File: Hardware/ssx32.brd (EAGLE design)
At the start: 61 x 60 mm, 81 parts, among them IC1 PIC18F45K20, IC2 FT232RL, IC3 TXB0108PW, IC4 TXB0108PW, IC5 TXB0108PW, IC6 TXB0108PW, IC7 78L33, IC8 74AHC1G32DBV, X1 8, X10 1, X11 19, X12 16, X13 15, X14 14, X15 13, X16 12, X17 11, X18 10, X19 9, X20 20, X21 21, X22 22, X23 23, X24 24, X25 25, X26 26, X27 27, X28 28, X29 29, X3 17, X30 30, X31 31, X32 32, X33 1751248, X34 18, X35 USB, X4 7, X5 6, X6 5, X7 4, X8 3, X9 2

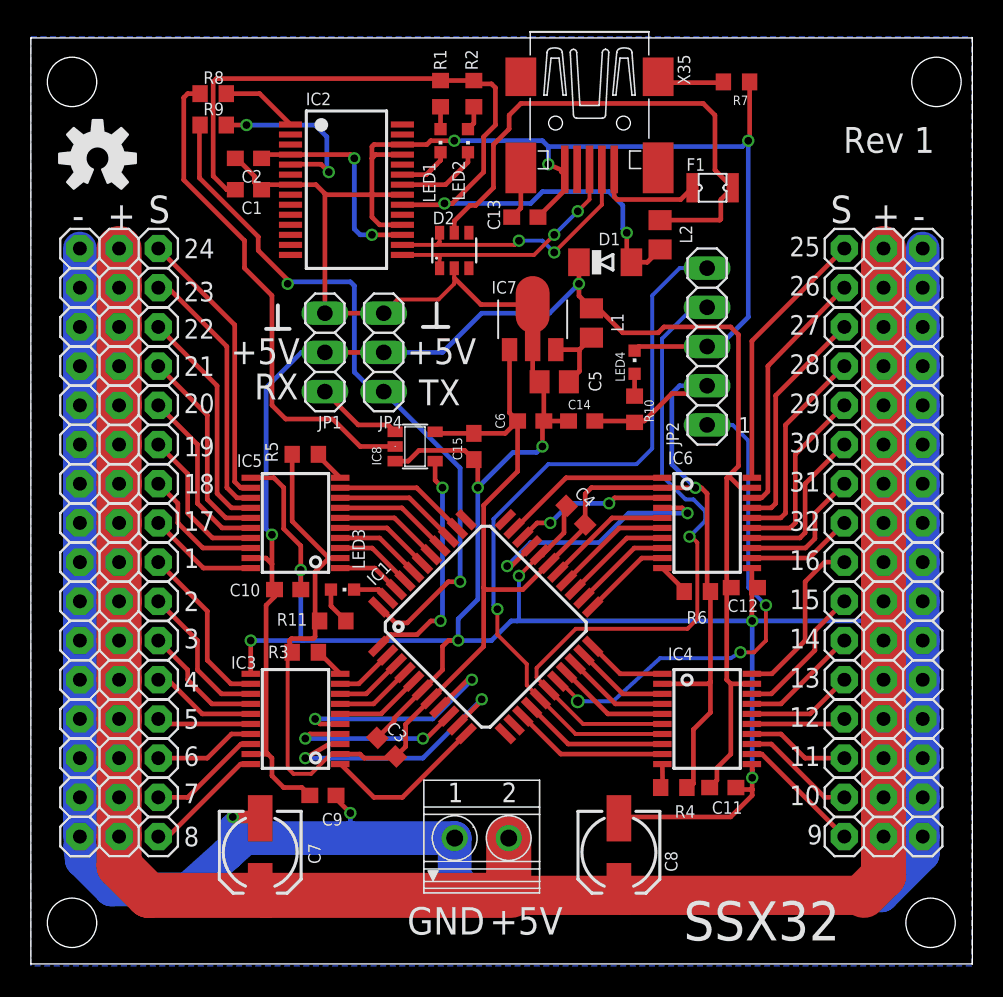
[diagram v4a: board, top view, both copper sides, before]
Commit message: Added software, minor board changes
Added software
Added resistor for not mounted ftdi chip
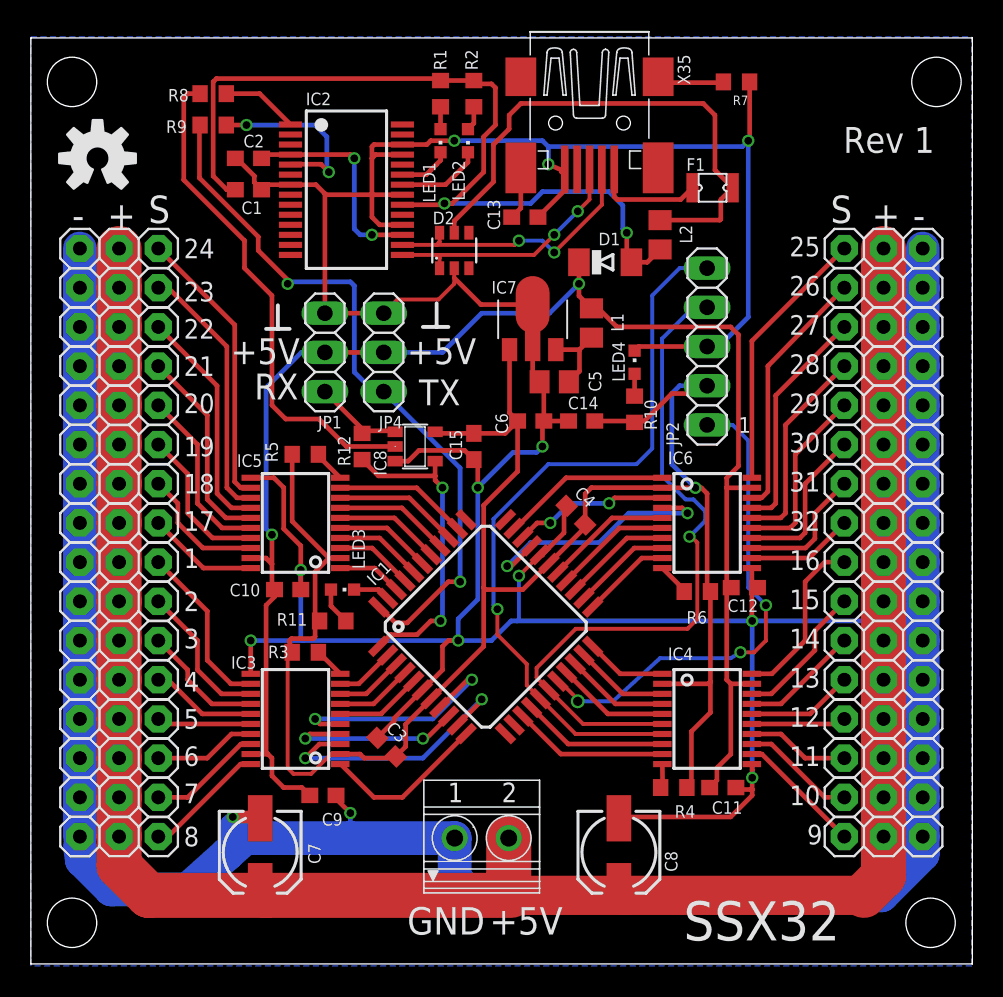
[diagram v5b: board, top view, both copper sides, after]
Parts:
- added R12: 0, rcl:R0603
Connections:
- net N$48: now also R12.1
- net N$54: now also R12.2
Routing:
- net N$48: track 15.3 -> 20.5 mm
- net +UB: track 102.6 -> 102.1 mm

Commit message: Revert "Added software, minor board changes"
This reverts commit cd959f70c37cd81d74ff6deb02d888d0a529ccba.
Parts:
- removed R12: 0, rcl:R0603
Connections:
- net N$48: no longer R12.1
- net N$54: no longer R12.2
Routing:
- net N$48: track 20.5 -> 15.3 mm
- net +UB: track 102.1 -> 102.6 mm

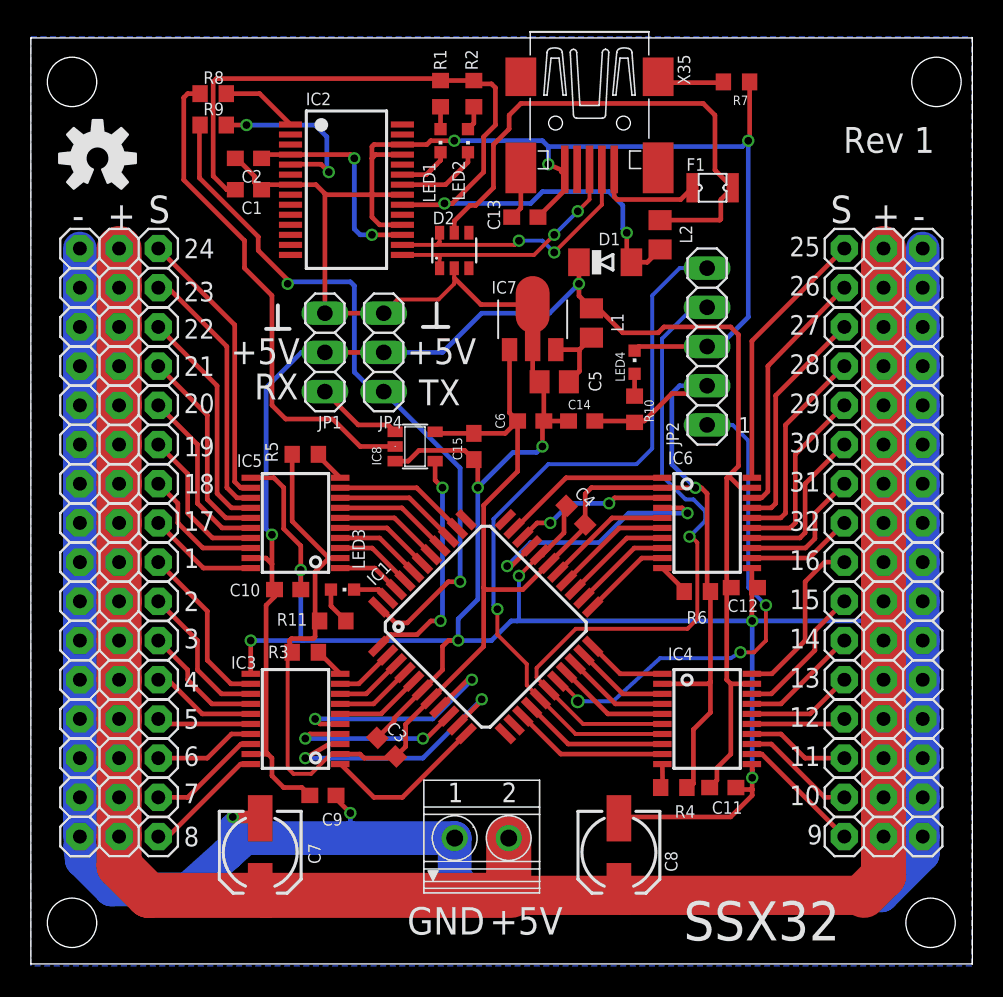
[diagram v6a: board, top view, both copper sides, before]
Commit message: Fixed issues
Replaced OR with AND gate with pullups
Removed unnecessary ferrite bead
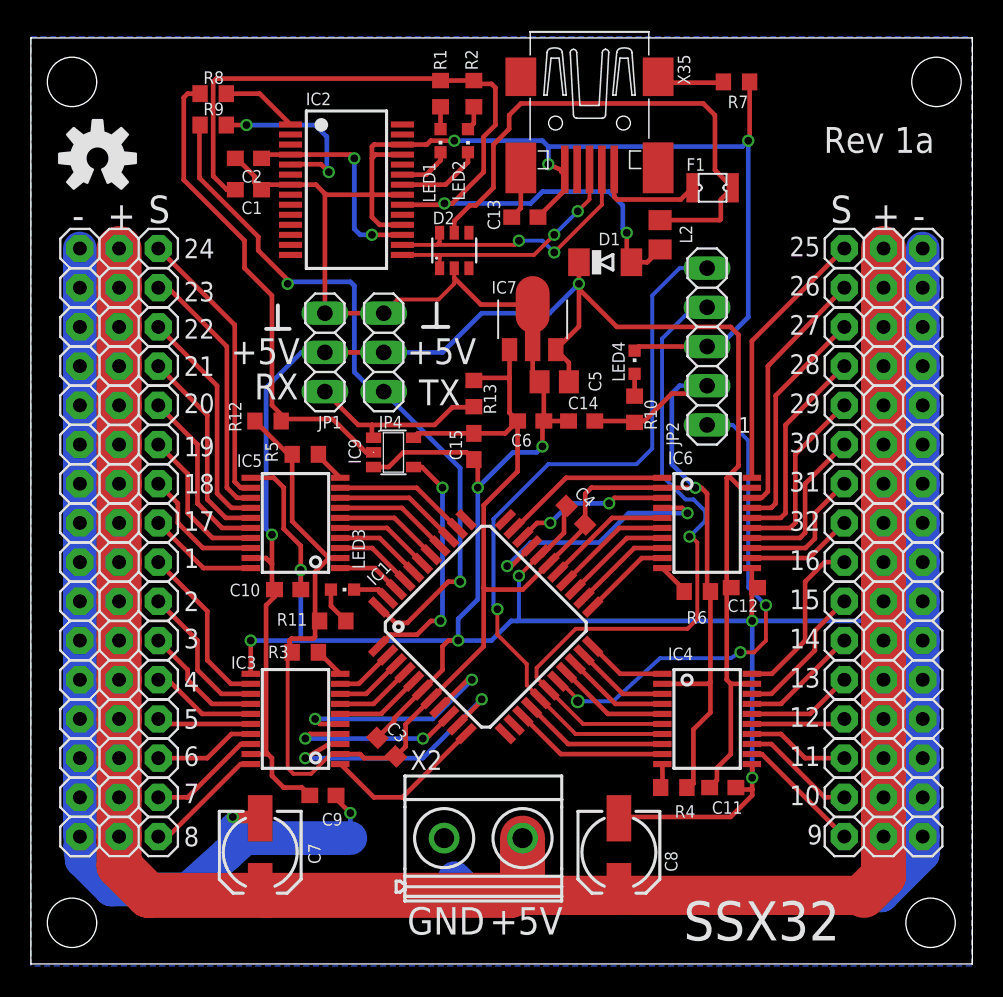
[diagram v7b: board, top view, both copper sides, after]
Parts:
- removed IC8: 74AHC1G32DBV, 74xx-little-de:SOT23-5
- removed L1: BLM21PG 300, rcl:R0805
- removed X33: 1751248, con-phoenix-350:1751248
- added IC9: 74LVC1G08DBV, 74xx-little-de:SOT23-5
- added R12, R13: 47k, rcl:R0603
- added X2: MKDSN1,5/2-5,08, con-phoenix-508:MKDSN1,5/2-5,08
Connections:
- removed net N$46: C5.2, IC7.3, L1.2
- net +3V3: now also IC9.5, R12.2, R13.1; no longer IC8.5
- net +UB: now also C5.2, IC7.3; no longer L1.1
- net GND: now also IC9.3, X2.1; no longer IC8.3, X33.1
- net N$48: now also IC9.4; no longer IC8.4
- net N$54: now also IC9.1, R13.2; no longer IC8.1
- net RX: now also IC9.2, R12.1; no longer IC8.2
- net VSERVO: now also X2.2; no longer X33.2
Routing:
- net GND: track 386.9 -> 379.0 mm
- net +3V3: track 128.2 -> 135.4 mm
- net +UB: track 102.6 -> 109.4 mm
- net N$54: track 5.63 -> 11.9 mm
- net N$46: track 5.00 -> 0.00 mm
- net RX: track 32.6 -> 31.6 mm
- net N$48: track 15.3 -> 15.8 mm
- net VSERVO: track 136.8 -> 137.3 mm
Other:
- board text added: "Rev 1a"
- board text removed: "Rev 1"
